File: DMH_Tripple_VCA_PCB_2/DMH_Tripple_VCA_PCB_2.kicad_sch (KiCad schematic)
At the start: 0 parts

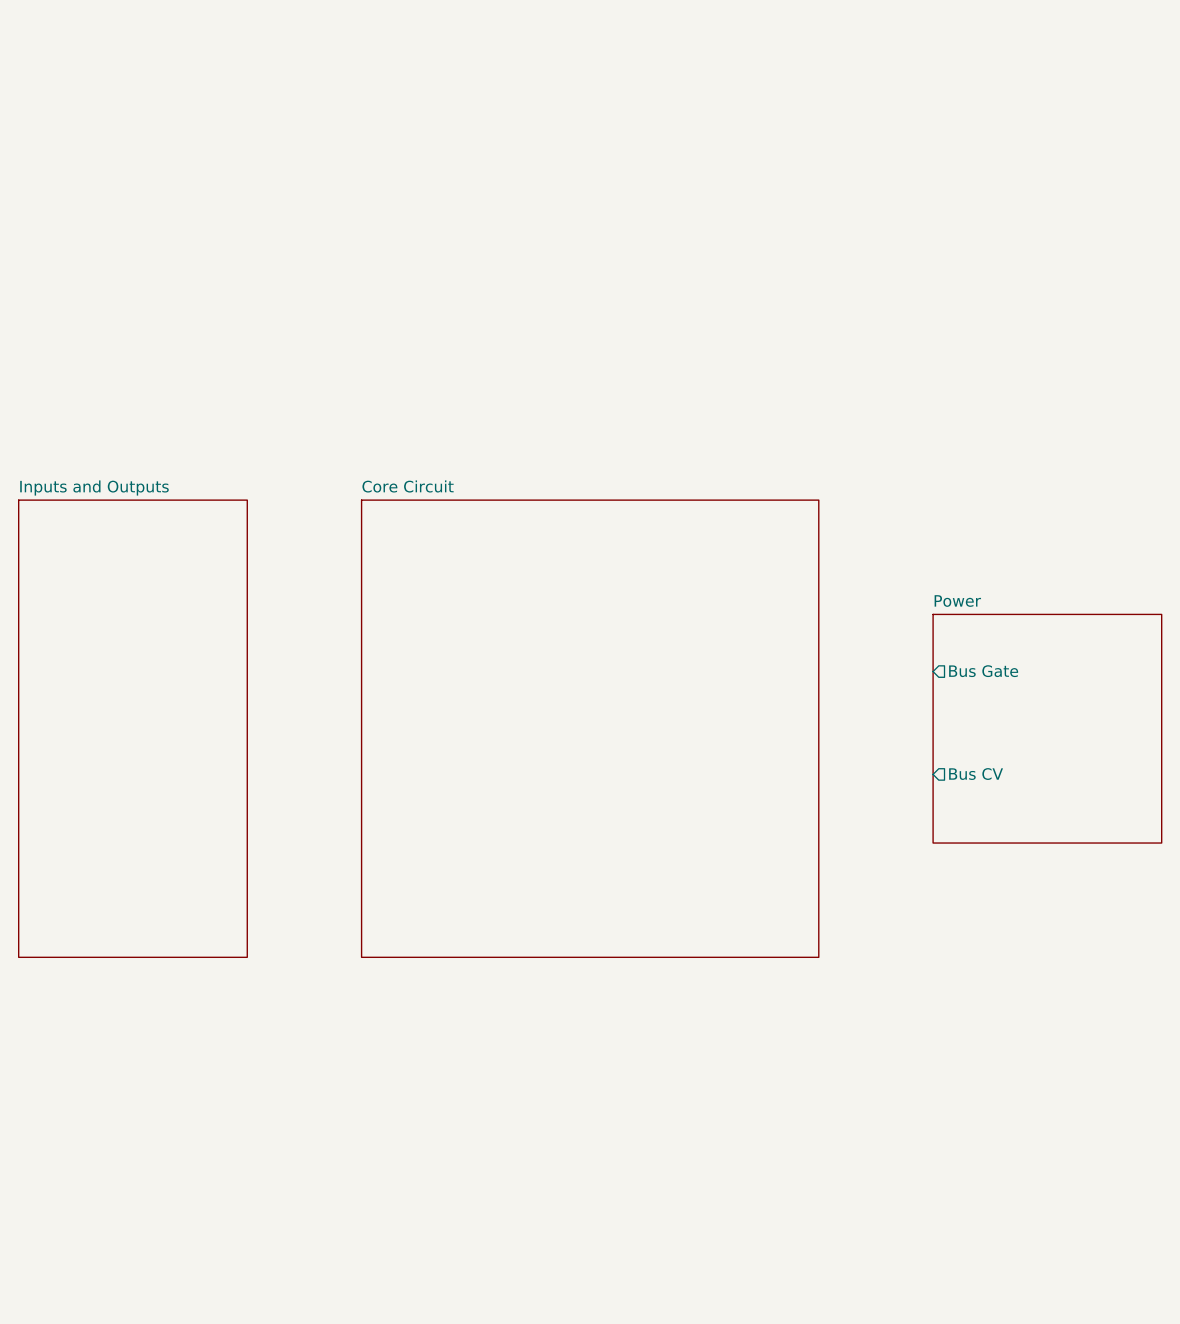
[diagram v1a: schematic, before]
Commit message: Corrected header locations and placed pcb2 comps
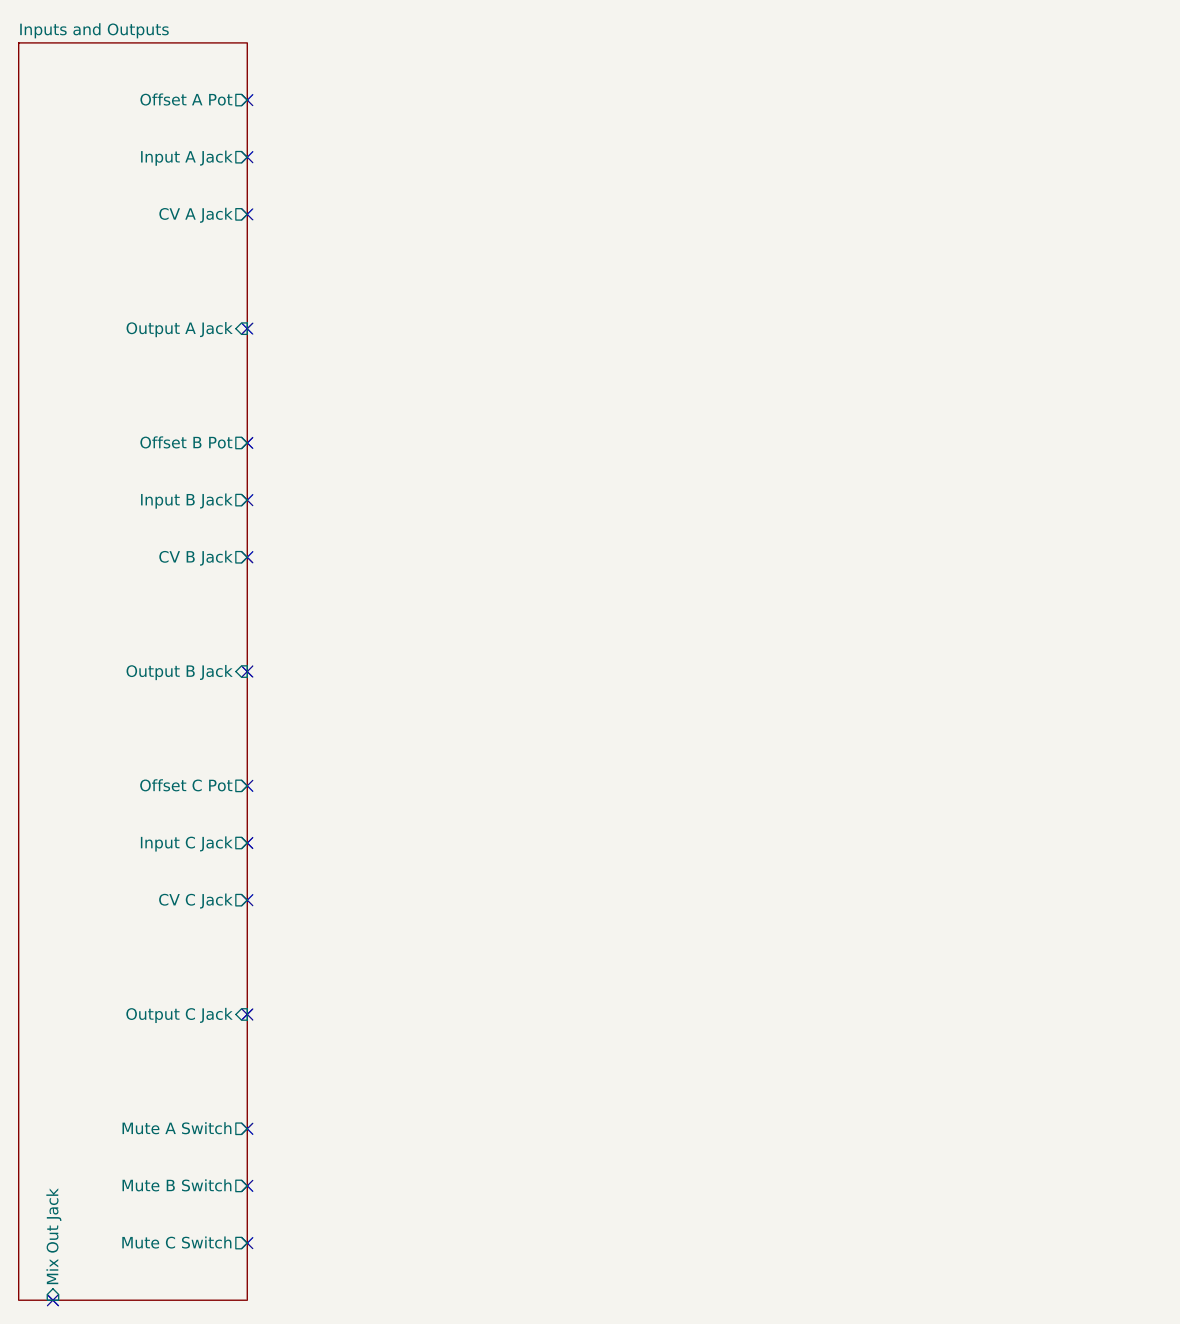
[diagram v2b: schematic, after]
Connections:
- no-connect marks 0 -> 16
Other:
- removed sheet Core Circuit
- removed sheet Power
- sheet Inputs and Outputs ports: added CV A Jack, CV B Jack, CV C Jack, Input A Jack, Input B Jack, Input C Jack, Mix Out Jack, Mute A Switch, Mute B Switch, Mute C Switch, Offset A Pot, Offset B Pot, Offset C Pot, Output A Jack, Output B Jack, Output C Jack; removed none
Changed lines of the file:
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@@
 		(comment 1 "PCB for 5 cm Kosmo format synthesizer module")
 	)
+	(no_connect
+		(at 50.8 44.45)
+	)
+	(no_connect
+		(at 50.8 69.85)
+	)
+	(no_connect
+		(at 50.8 158.75)
+	)
+	(no_connect
+		(at 50.8 120.65)
+	)
+	(no_connect
+		(at 50.8 107.95)
+	)
+	(no_connect
+		(at 50.8 152.4)
+	)
+	(no_connect
+		(at 50.8 114.3)
+	)
+	(no_connect
+		(at 50.8 95.25)
+	)
+	(no_connect
+		(at 50.8 38.1)
+	)
+	(no_connect
+		(at 50.8 146.05)
+	)
+	(no_connect
+		(at 29.21 165.1)
+	)
+	(no_connect
+		(at 50.8 57.15)
+	)
+	(no_connect
+		(at 50.8 133.35)
+	)
+	(no_connect
+		(at 50.8 82.55)
+	)
+	(no_connect
+		(at 50.8 31.75)
+	)
+	(no_connect
+		(at 50.8 76.2)
+	)
 	(sheet
-		(at 127 88.9)
-		(size 25.4 25.4)
+		(at 25.4 25.4)
+		(size 25.4 139.7)
 		(exclude_from_sim no)
 		(in_bom yes)
@@
 			(color 0 0 0 0.0000)
 		)
-		(property "Sheetname" "Power"
-			(at 127 88.1884 0)
+		(property "Sheetname" "Inputs and Outputs"
+			(at 25.4 24.6884 0)
 			(effects
 				(font
@@
 			)
 		)
-		(property "Sheetfile" "Power.kicad_sch"
-			(at 127 114.8846 0)
+		(property "Sheetfile" "Inputs_and_Outputs.kicad_sch"
+			(at 25.4 165.6846 0)
 			(effects
 				(font
@@
 			)
 		)
-		(pin "Bus Gate" output
-			(at 127 95.25 180)
+		(pin "CV A Jack" output
+			(at 50.8 44.45 0)
+			(effects
+				(font
+					(size 1.27 1.27)
+				)
+				(justify right)
+			)
+		)
+		(pin "CV B Jack" output
+			(at 50.8 82.55 0)
+			(effects
+				(font
+					(size 1.27 1.27)
+				)
+				(justify right)
+			)
+		)
+		(pin "CV C Jack" output
+			(at 50.8 120.65 0)
+			(effects
+				(font
+					(size 1.27 1.27)
+				)
+				(justify right)
+			)
+		)
+		(pin "Input A Jack" output
+			(at 50.8 38.1 0)
+			(effects
+				(font
+					(size 1.27 1.27)
+				)
+				(justify right)
+			)
+		)
+		(pin "Input B Jack" output
+			(at 50.8 76.2 0)
+			(effects
+				(font
+					(size 1.27 1.27)
+				)
+				(justify right)
+			)
+		)
+		(pin "Input C Jack" output
+			(at 50.8 114.3 0)
+			(effects
+				(font
+					(size 1.27 1.27)
+				)
+				(justify right)
+			)
+		)
+		(pin "Mix Out Jack" input
+			(at 29.21 165.1 270)
 			(effects
 				(font
@@
 			)
 		)
-		(pin "Bus CV" output
-			(at 127 106.68 180)
-			(effects
-				(font
-					(size 1.27 1.27)
-				)
-				(justify left)
-			)
-		)
-		(instances
-			(project "DMH_Tripple_VCA_PCB_2"
-				(path "/58f4306d-5387-4983-bb08-41a2313fd315"
-					(page "4")
-				)
-			)
-		)
-	)
-	(sheet
-		(at 63.5 76.2)
-		(size 50.8 50.8)
-		(exclude_from_sim no)
-		(in_bom yes)
-		(on_board yes)
-		(dnp no)
-		(fields_autoplaced yes)
-		(stroke
-			(width 0.1524)
-			(type solid)
-		)
-		(fill
-			(color 0 0 0 0.0000)
-		)
-		(property "Sheetname" "Core Circuit"
-			(at 63.5 75.4884 0)
-			(effects
-				(font
-					(size 1.27 1.27)
-				)
-				(justify left bottom)
-			)
-		)
-		(property "Sheetfile" "Core_Circuit.kicad_sch"
-			(at 63.5 127.5846 0)
-			(effects
-				(font
-					(size 1.27 1.27)
-				)
-				(justify left top)
-				(hide yes)
-			)
-		)
-		(instances
-			(project "DMH_Tripple_VCA_PCB_2"
-				(path "/58f4306d-5387-4983-bb08-41a2313fd315"
-					(page "3")
-				)
-			)
-		)
-	)
-	(sheet
-		(at 25.4 76.2)
-		(size 25.4 50.8)
-		(exclude_from_sim no)
-		(in_bom yes)
-		(on_board yes)
-		(dnp no)
-		(fields_autoplaced yes)
-		(stroke
-			(width 0.1524)
-			(type solid)
-		)
-		(fill
-			(color 0 0 0 0.0000)
-		)
-		(property "Sheetname" "Inputs and Outputs"
-			(at 25.4 75.4884 0)
-			(effects
-				(font
-					(size 1.27 1.27)
-				)
-				(justify left bottom)
-			)
-		)
-		(property "Sheetfile" "Inputs_and_Outputs.kicad_sch"
-			(at 25.4 127.5846 0)
-			(effects
-				(font
-					(size 1.27 1.27)
-				)
-				(justify left top)
-				(hide yes)
-			)
-		)
+		(pin "Mute A Switch" output
+			(at 50.8 146.05 0)
+			(effects
+				(font
+					(size 1.27 1.27)
+				)
+				(justify right)
+			)
+		)
+		(pin "Mute B Switch" output
+			(at 50.8 152.4 0)
+			(effects
+				(font
+					(size 1.27 1.27)
+				)
+				(justify right)
+			)
+		)
+		(pin "Mute C Switch" output
+			(at 50.8 158.75 0)
+			(effects
+				(font
+					(size 1.27 1.27)
+				)
+				(justify right)
+			)
+		)
+		(pin "Offset A Pot" output
+			(at 50.8 31.75 0)
+			(effects
+				(font
+					(size 1.27 1.27)
+				)
+				(justify right)
+			)
+		)
+		(pin "Offset B Pot" output
+			(at 50.8 69.85 0)
+			(effects
+				(font
+					(size 1.27 1.27)
+				)
+				(justify right)
+			)
+		)
+		(pin "Offset C Pot" output
+			(at 50.8 107.95 0)
+			(effects
+				(font
+					(size 1.27 1.27)
+				)
+				(justify right)
+			)
+		)
+		(pin "Output A Jack" input
+			(at 50.8 57.15 0)
+			(effects
+				(font
+					(size 1.27 1.27)
+				)
+				(justify right)
+			)
+		)
+		(pin "Output B Jack" input
+			(at 50.8 95.25 0)
+			(effects
+				(font
+					(size 1.27 1.27)
+				)
+				(justify right)
+			)
+		)
+		(pin "Output C Jack" input
+			(at 50.8 133.35 0)
+			(effects
+				(font
+					(size 1.27 1.27)
+				)
+				(justify right)
+			)
+		)
